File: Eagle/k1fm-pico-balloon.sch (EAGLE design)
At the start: 42 parts, among them J1 I2C, J2 ICSP, J3 SERIAL, J4 POWER, Q1 ASTX-H11-25.000MHZ-T, Q2 DMP2305U, Q3 DMP2305U, U1 ATMEGA328, U2 Si5351A-B-GT, U3 MCP1754X-XXXXX/C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

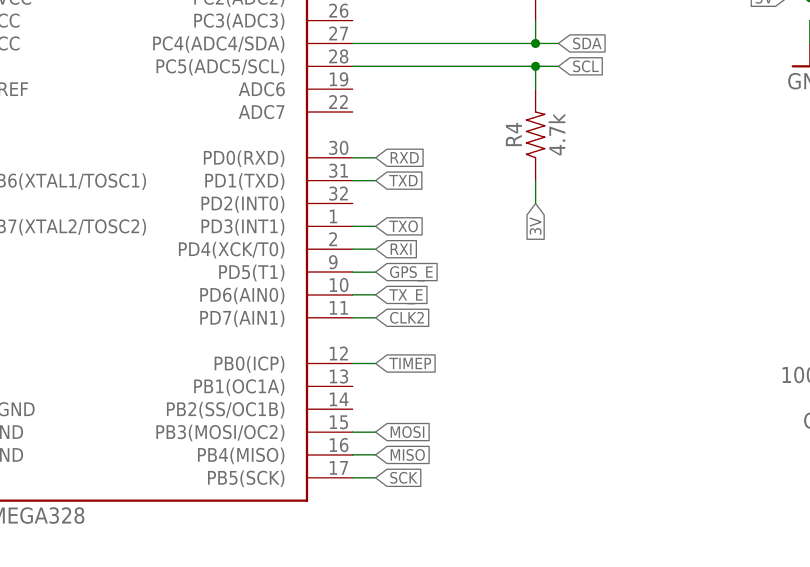
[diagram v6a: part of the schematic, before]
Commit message: Use PD2 (ext int) and PD5 (T1) for calibration
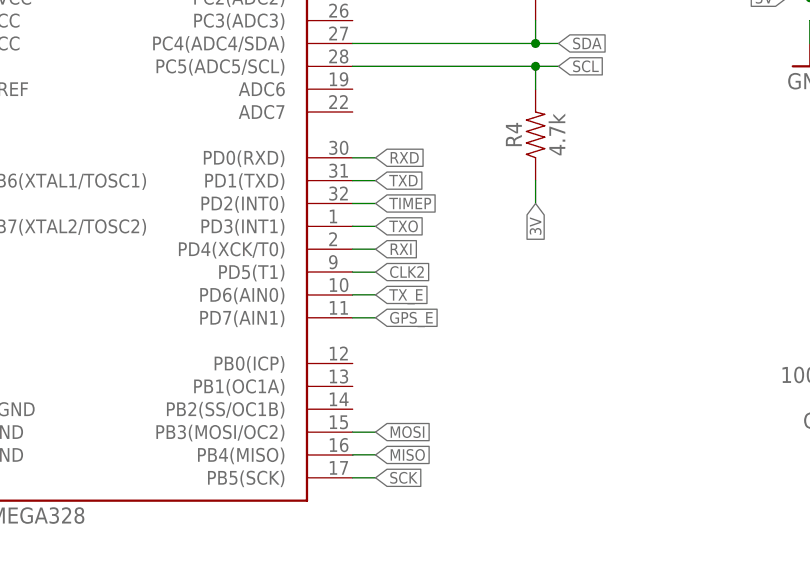
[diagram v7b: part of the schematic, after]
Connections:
- net CLK2: now also U1.PD5(T1); no longer U1.PD7(AIN1)
- net GPS_E: now also U1.PD7(AIN1); no longer U1.PD5(T1)
- net TIMEP: now also U1.PD2(INT0); no longer U1.PB0(ICP)
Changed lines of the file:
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@@
 <net name="GPS_E" class="0">
-<segment>
-<pinref part="U1" gate="G$1" pin="PD5(T1)"/>
-<wire x1="157.48" y1="78.74" x2="160.02" y2="78.74" width="0.1524" layer="91"/>
-<label x="160.02" y="78.74" size="1.27" layer="95" xref="yes"/>
-</segment>
 <segment>
 <pinref part="R6" gate="G$1" pin="1"/>
@@
 <junction x="259.08" y="190.5"/>
 <label x="261.62" y="190.5" size="1.778" layer="95" xref="yes"/>
+</segment>
+<segment>
+<pinref part="U1" gate="G$1" pin="PD7(AIN1)"/>
+<wire x1="157.48" y1="73.66" x2="160.02" y2="73.66" width="0.1524" layer="91"/>
+<label x="160.02" y="73.66" size="1.27" layer="95" xref="yes"/>
 </segment>
 </net>
@@
 </segment>
 <segment>
-<pinref part="U1" gate="G$1" pin="PD7(AIN1)"/>
-<wire x1="157.48" y1="73.66" x2="160.02" y2="73.66" width="0.1524" layer="91"/>
-<label x="160.02" y="73.66" size="1.27" layer="95" xref="yes"/>
+<pinref part="U1" gate="G$1" pin="PD5(T1)"/>
+<wire x1="157.48" y1="78.74" x2="160.02" y2="78.74" width="0.1524" layer="91"/>
+<label x="160.02" y="78.74" size="1.27" layer="95" xref="yes"/>
 </segment>
 </net>
@@
 </segment>
 <segment>
-<pinref part="U1" gate="G$1" pin="PB0(ICP)"/>
-<wire x1="157.48" y1="68.58" x2="160.02" y2="68.58" width="0.1524" layer="91"/>
-<label x="160.02" y="68.58" size="1.27" layer="95" xref="yes"/>
+<pinref part="U1" gate="G$1" pin="PD2(INT0)"/>
+<wire x1="157.48" y1="86.36" x2="160.02" y2="86.36" width="0.1524" layer="91"/>
+<label x="160.02" y="86.36" size="1.27" layer="95" xref="yes"/>
 </segment>
 </net>

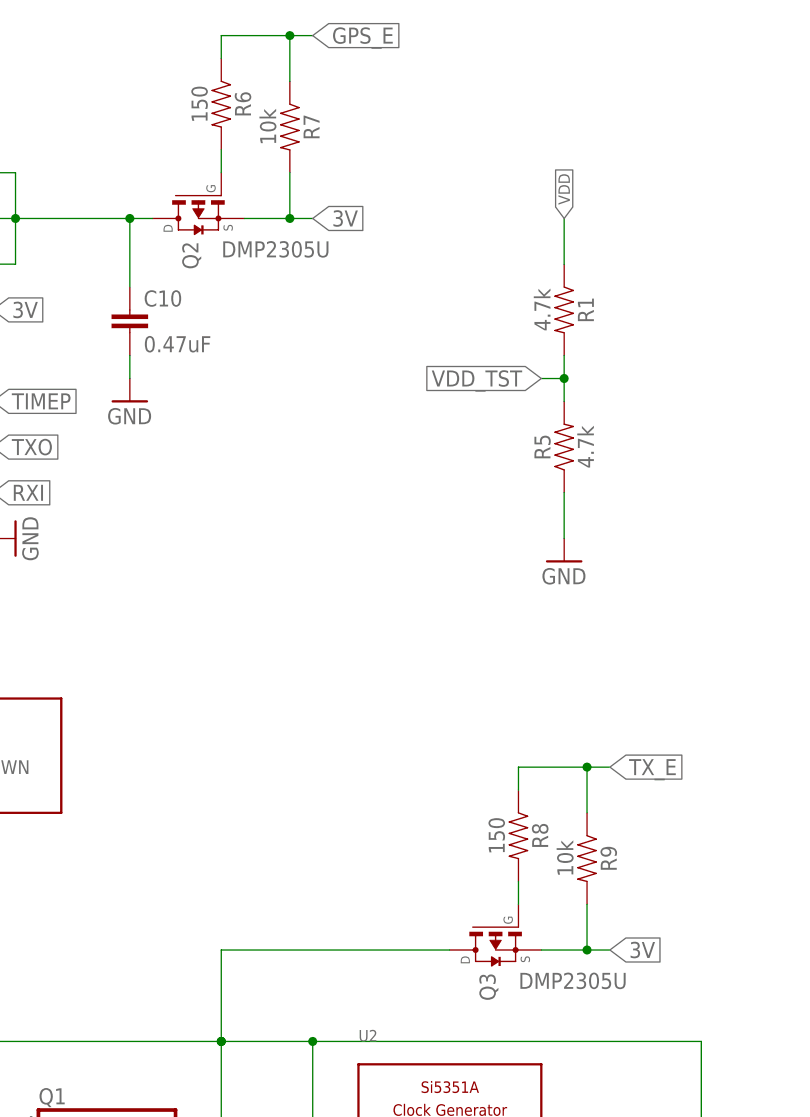
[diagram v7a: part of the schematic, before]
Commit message: Fix Mosfet polarization
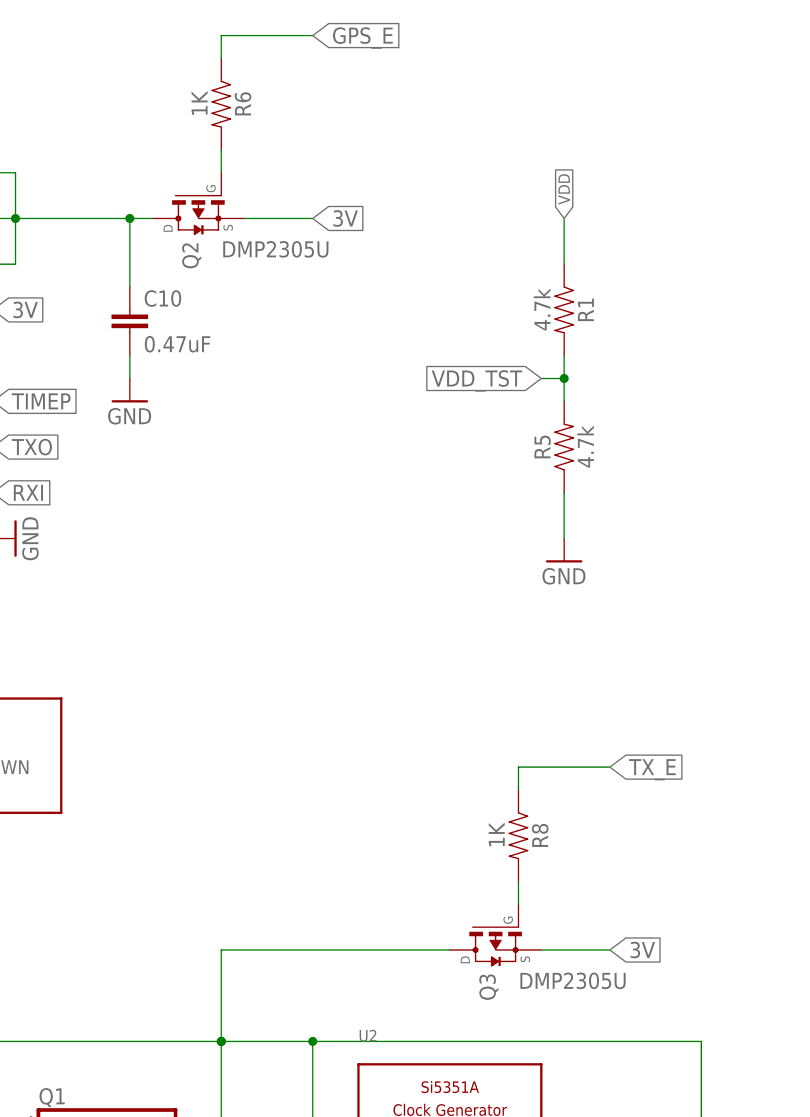
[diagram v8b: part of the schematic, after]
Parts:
- removed R7, R9: 10k, SparkFun-Resistors:10KOHM-0603-1/10W-1%
- R6, R8: value 150 -> 1K
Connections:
- net 3V: no longer R7.2, R9.2
- net GPS_E: no longer R7.1
- net TX_E: no longer R9.1
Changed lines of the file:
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@@
 <part name="GND23" library="SparkFun" deviceset="GND" device=""/>
 <part name="Q2" library="transistor-fet" deviceset="DMP2305U" device=""/>
-<part name="R6" library="SparkFun-Resistors" library_urn="urn:adsk.eagle:library:532" deviceset="10KOHM" device="-0603-1/10W-1%" package3d_urn="urn:adsk.eagle:package:39650/1" value="150"/>
-<part name="R7" library="SparkFun-Resistors" library_urn="urn:adsk.eagle:library:532" deviceset="10KOHM" device="-0603-1/10W-1%" package3d_urn="urn:adsk.eagle:package:39650/1" value="10k"/>
+<part name="R6" library="SparkFun-Resistors" library_urn="urn:adsk.eagle:library:532" deviceset="10KOHM" device="-0603-1/10W-1%" package3d_urn="urn:adsk.eagle:package:39650/1" value="1K"/>
 <part name="C13" library="SparkFun-Capacitors" library_urn="urn:adsk.eagle:library:510" deviceset="10NF" device="-0603-50V-10%" package3d_urn="urn:adsk.eagle:package:37414/1" value="10nF"/>
 <part name="HF-ANT" library="SparkFun-Connectors" library_urn="urn:adsk.eagle:library:513" deviceset="CONN_02" device="" package3d_urn="urn:adsk.eagle:package:38039/1" value="HF ANT"/>
 <part name="GND24" library="supply1" deviceset="GND" device=""/>
 <part name="Q3" library="transistor-fet" deviceset="DMP2305U" device=""/>
-<part name="R8" library="SparkFun-Resistors" library_urn="urn:adsk.eagle:library:532" deviceset="10KOHM" device="-0603-1/10W-1%" package3d_urn="urn:adsk.eagle:package:39650/1" value="150"/>
-<part name="R9" library="SparkFun-Resistors" library_urn="urn:adsk.eagle:library:532" deviceset="10KOHM" device="-0603-1/10W-1%" package3d_urn="urn:adsk.eagle:package:39650/1" value="10k"/>
+<part name="R8" library="SparkFun-Resistors" library_urn="urn:adsk.eagle:library:532" deviceset="10KOHM" device="-0603-1/10W-1%" package3d_urn="urn:adsk.eagle:package:39650/1" value="1K"/>
 <part name="C14" library="SparkFun-Capacitors" library_urn="urn:adsk.eagle:library:510" deviceset="10NF" device="-0603-50V-10%" package3d_urn="urn:adsk.eagle:package:37414/1" value="100nF"/>
 <part name="GND25" library="SparkFun-Aesthetics" library_urn="urn:adsk.eagle:library:507" deviceset="GND" device=""/>
@@
 <attribute name="VALUE" x="249.936" y="182.88" size="1.778" layer="96" font="vector" rot="R270" align="top-center"/>
 </instance>
-<instance part="R7" gate="G$1" x="259.08" y="180.34" smashed="yes" rot="R270">
-<attribute name="NAME" x="260.604" y="180.34" size="1.778" layer="95" font="vector" rot="R270" align="bottom-center"/>
-<attribute name="VALUE" x="257.556" y="180.34" size="1.778" layer="96" font="vector" rot="R270" align="top-center"/>
-</instance>
 <instance part="C13" gate="G$1" x="259.08" y="63.5" smashed="yes" rot="R90">
 <attribute name="NAME" x="256.159" y="65.024" size="1.778" layer="95" font="vector" rot="R90"/>
@@
 <attribute name="NAME" x="286.004" y="101.6" size="1.778" layer="95" font="vector" rot="R270" align="bottom-center"/>
 <attribute name="VALUE" x="282.956" y="101.6" size="1.778" layer="96" font="vector" rot="R270" align="top-center"/>
-</instance>
-<instance part="R9" gate="G$1" x="292.1" y="99.06" smashed="yes" rot="R270">
-<attribute name="NAME" x="293.624" y="99.06" size="1.778" layer="95" font="vector" rot="R270" align="bottom-center"/>
-<attribute name="VALUE" x="290.576" y="99.06" size="1.778" layer="96" font="vector" rot="R270" align="top-center"/>
 </instance>
 <instance part="C14" gate="G$1" x="213.36" y="66.04" smashed="yes" rot="R180">
@@
 <segment>
 <pinref part="Q3" gate="G$1" pin="S"/>
-<wire x1="287.02" y1="88.9" x2="292.1" y2="88.9" width="0.1524" layer="91"/>
-<pinref part="R9" gate="G$1" pin="2"/>
-<wire x1="292.1" y1="93.98" x2="292.1" y2="88.9" width="0.1524" layer="91"/>
-<wire x1="292.1" y1="88.9" x2="294.64" y2="88.9" width="0.1524" layer="91"/>
-<junction x="292.1" y="88.9"/>
+<wire x1="287.02" y1="88.9" x2="294.64" y2="88.9" width="0.1524" layer="91"/>
 <label x="294.64" y="88.9" size="1.778" layer="95" xref="yes"/>
 </segment>
 <segment>
 <pinref part="Q2" gate="G$1" pin="S"/>
-<wire x1="254" y1="170.18" x2="259.08" y2="170.18" width="0.1524" layer="91"/>
-<pinref part="R7" gate="G$1" pin="2"/>
-<wire x1="259.08" y1="175.26" x2="259.08" y2="170.18" width="0.1524" layer="91"/>
-<wire x1="259.08" y1="170.18" x2="261.62" y2="170.18" width="0.1524" layer="91"/>
-<junction x="259.08" y="170.18"/>
+<wire x1="254" y1="170.18" x2="261.62" y2="170.18" width="0.1524" layer="91"/>
 <label x="261.62" y="170.18" size="1.778" layer="95" xref="yes"/>
 </segment>
@@
 <pinref part="R6" gate="G$1" pin="1"/>
 <wire x1="251.46" y1="187.96" x2="251.46" y2="190.5" width="0.1524" layer="91"/>
-<wire x1="251.46" y1="190.5" x2="259.08" y2="190.5" width="0.1524" layer="91"/>
-<pinref part="R7" gate="G$1" pin="1"/>
-<wire x1="259.08" y1="190.5" x2="259.08" y2="185.42" width="0.1524" layer="91"/>
-<wire x1="259.08" y1="190.5" x2="261.62" y2="190.5" width="0.1524" layer="91"/>
-<junction x="259.08" y="190.5"/>
+<wire x1="251.46" y1="190.5" x2="261.62" y2="190.5" width="0.1524" layer="91"/>
 <label x="261.62" y="190.5" size="1.778" layer="95" xref="yes"/>
 </segment>
@@
 <pinref part="R8" gate="G$1" pin="1"/>
 <wire x1="284.48" y1="106.68" x2="284.48" y2="109.22" width="0.1524" layer="91"/>
-<wire x1="284.48" y1="109.22" x2="292.1" y2="109.22" width="0.1524" layer="91"/>
-<pinref part="R9" gate="G$1" pin="1"/>
-<wire x1="292.1" y1="109.22" x2="292.1" y2="104.14" width="0.1524" layer="91"/>
-<wire x1="292.1" y1="109.22" x2="294.64" y2="109.22" width="0.1524" layer="91"/>
-<junction x="292.1" y="109.22"/>
+<wire x1="284.48" y1="109.22" x2="294.64" y2="109.22" width="0.1524" layer="91"/>
 <label x="294.64" y="109.22" size="1.778" layer="95" xref="yes"/>
 </segment>
